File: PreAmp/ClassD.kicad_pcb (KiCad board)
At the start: 2 copper layers, 41 parts, among them J1 Conn_01x02_Pin, J2 Conn_01x02_Pin, J3 Conn_01x03, U1 L78L09_TO92, U2 LM358, U3 TL494

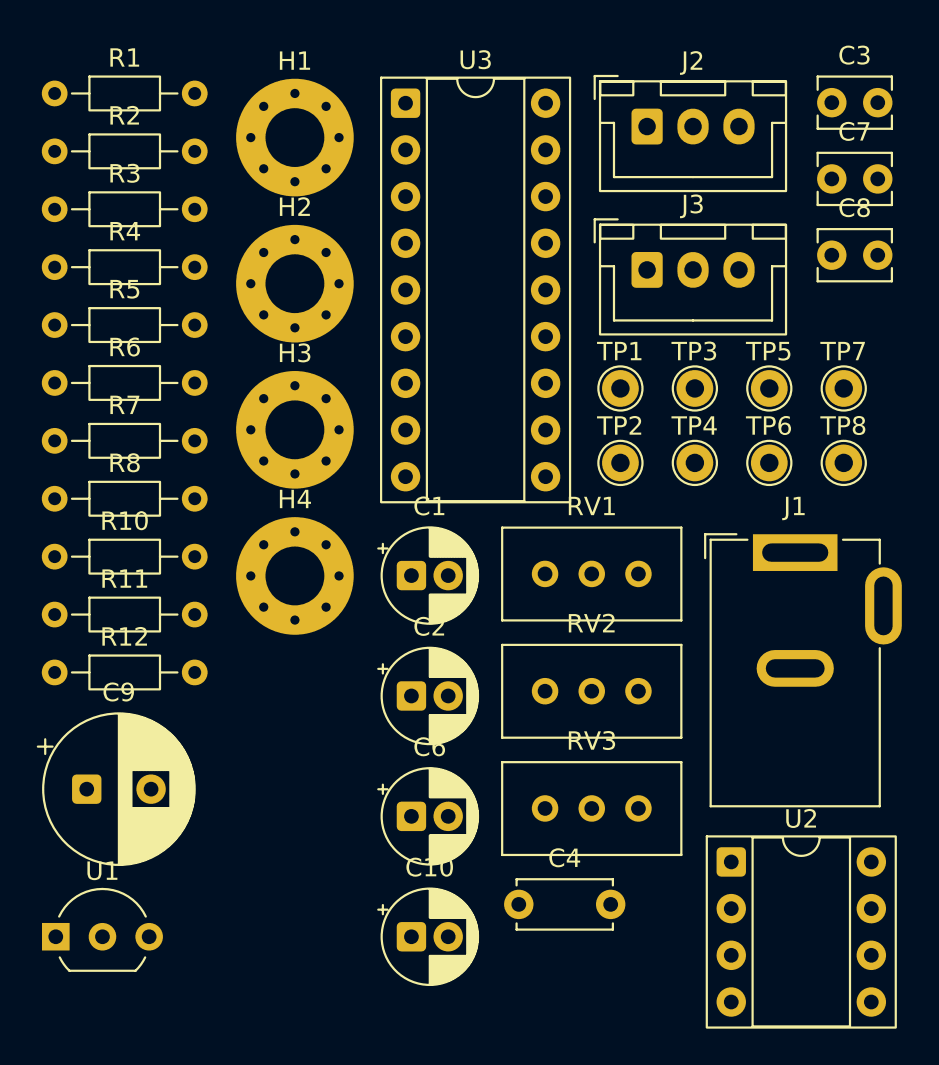
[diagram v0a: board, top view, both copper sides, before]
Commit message: Fixed audio jack to 2 pins
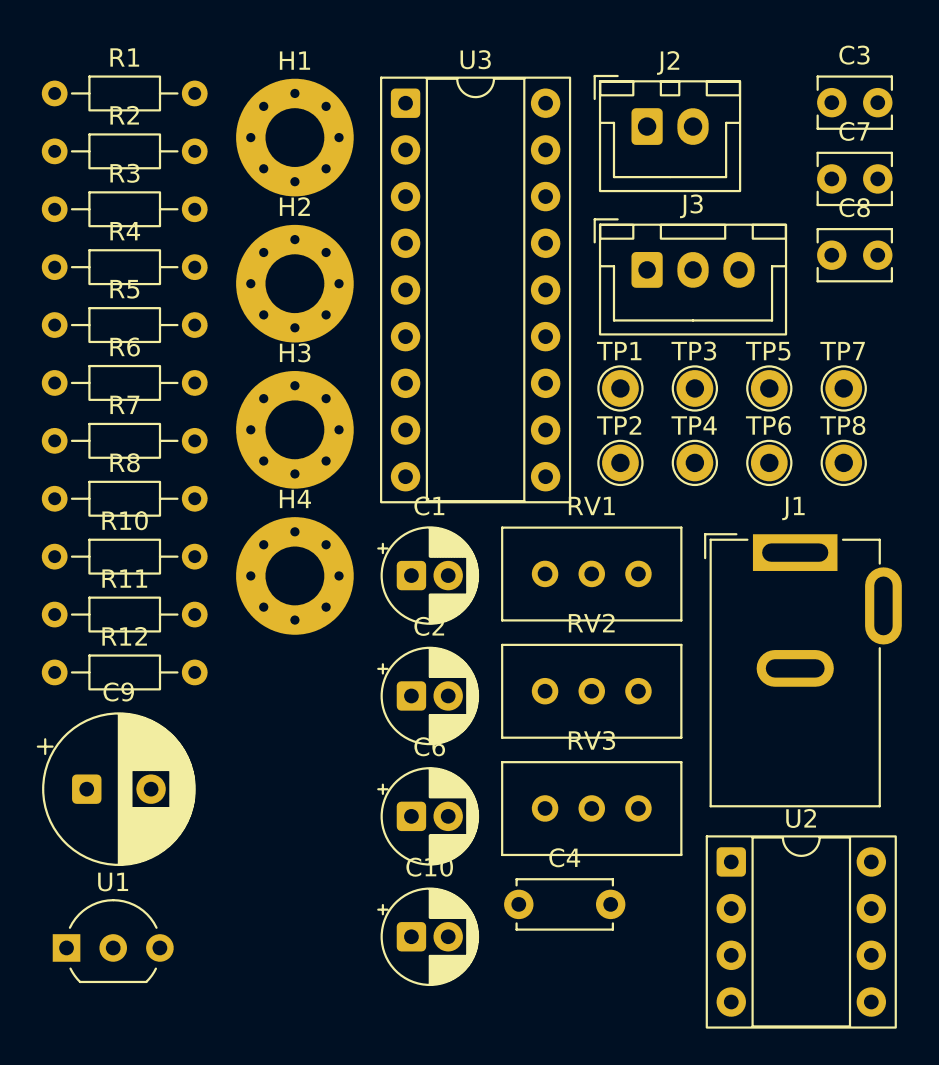
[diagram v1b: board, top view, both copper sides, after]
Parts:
- J2: footprint Connector_JST:JST_XH_B3B-XH-A_1x03_P2.50mm_Vertical -> Connector_JST:JST_XH_B2B-XH-A_1x02_P2.50mm_Vertical
- moved U1 0.85 mm to (59.7, 67.9)
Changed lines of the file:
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@@
 		(legacy_teardrops no)
 	)
-	(paper "User" 160 120)
+	(paper "User" 200 160)
 	(layers
 		(0 "F.Cu" signal)
@@
 	(footprint "Package_TO_SOT_THT:TO-92_Inline_Wide"
 		(layer "F.Cu")
-		(at 59.105 67.335)
+		(at 59.69 67.945)
 		(descr "TO-92 leads in-line, wide, drill 0.75mm (see NXP sot054_po.pdf)")
 		(tags "to-92 sc-43 sc-43a sot54 PA33 transistor")
@@
 		(embedded_fonts no)
 	)
-	(footprint "Connector_JST:JST_XH_B3B-XH-A_1x03_P2.50mm_Vertical"
+	(footprint "Connector_JST:JST_XH_B2B-XH-A_1x02_P2.50mm_Vertical"
 		(layer "F.Cu")
 		(at 91.275 23.255)
-		(descr "JST XH series connector, B3B-XH-A (http://www.jst-mfg.com/product/pdf/eng/eXH.pdf), generated with kicad-footprint-generator")
+		(descr "JST XH series connector, B2B-XH-A (http://www.jst-mfg.com/product/pdf/eng/eXH.pdf), generated with kicad-footprint-generator")
 		(tags "connector JST XH vertical")
 		(property "Reference" "J2"
-			(at 2.5 -3.55 0)
+			(at 1.25 -3.55 0)
 			(layer "F.SilkS")
 			(effects
@@
 		)
 		(property "Value" "Conn_01x02_Pin"
-			(at 2.5 4.6 0)
+			(at 1.25 4.6 0)
 			(layer "F.Fab")
 			(effects
@@
 		(fp_line
 			(start -1.8 2.75)
-			(end 2.5 2.75)
+			(end 1.25 2.75)
 			(stroke
 				(width 0.12)
@@
 		)
 		(fp_line
-			(start 6.8 -0.2)
-			(end 6.8 2.75)
+			(start 4.3 -0.2)
+			(end 4.3 2.75)
 			(stroke
 				(width 0.12)
@@
 		)
 		(fp_line
-			(start 6.8 2.75)
-			(end 2.5 2.75)
+			(start 4.3 2.75)
+			(end 1.25 2.75)
 			(stroke
 				(width 0.12)
@@
 		)
 		(fp_line
-			(start 7.55 -0.2)
-			(end 6.8 -0.2)
+			(start 5.05 -0.2)
+			(end 4.3 -0.2)
 			(stroke
 				(width 0.12)
@@
 		(fp_rect
 			(start -2.56 -2.46)
-			(end 7.56 3.51)
+			(end 5.06 3.51)
 			(stroke
 				(width 0.12)
@@
 		(fp_rect
 			(start 0.75 -2.45)
-			(end 4.25 -1.7)
+			(end 1.75 -1.7)
 			(stroke
 				(width 0.12)
@@
 		)
 		(fp_rect
-			(start 5.75 -2.45)
-			(end 7.55 -1.7)
+			(start 3.25 -2.45)
+			(end 5.05 -1.7)
 			(stroke
 				(width 0.12)
@@
 		(fp_rect
 			(start -2.95 -2.85)
-			(end 7.95 3.9)
+			(end 5.45 3.9)
 			(stroke
 				(width 0.05)
@@
 		(fp_rect
 			(start -2.45 -2.35)
-			(end 7.45 3.4)
+			(end 4.95 3.4)
 			(stroke
 				(width 0.1)
@@
 		)
 		(fp_text user "${REFERENCE}"
-			(at 2.5 2.7 0)
+			(at 1.25 2.7 0)
 			(layer "F.Fab")
 			(effects
@@
 		(pad "1" thru_hole roundrect
 			(at 0 0)
-			(size 1.7 1.95)
-			(drill 0.95)
+			(size 1.7 2)
+			(drill 1)
 			(layers "*.Cu" "*.Mask")
 			(remove_unused_layers no)
@@
 		(pad "2" thru_hole oval
 			(at 2.5 0)
-			(size 1.7 1.95)
-			(drill 0.95)
+			(size 1.7 2)
+			(drill 1)
 			(layers "*.Cu" "*.Mask")
 			(remove_unused_layers no)
@@
 			(pintype "passive")
 		)
-		(pad "3" thru_hole oval
-			(at 5 0)
-			(size 1.7 1.95)
-			(drill 0.95)
-			(layers "*.Cu" "*.Mask")
-			(remove_unused_layers no)
-		)
 		(embedded_fonts no)
-		(model "${KICAD9_3DMODEL_DIR}/Connector_JST.3dshapes/JST_XH_B3B-XH-A_1x03_P2.50mm_Vertical.step"
+		(model "${KICAD9_3DMODEL_DIR}/Connector_JST.3dshapes/JST_XH_B2B-XH-A_1x02_P2.50mm_Vertical.step"
 			(offset
 				(xyz 0 0 0)
